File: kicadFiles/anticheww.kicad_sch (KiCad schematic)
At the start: 436 parts, among them J1 ARM JTAG, J2 TYPE-C-31-M-12, J3 Conn_02x05_Odd_Even, Q1 AO3401A, Q2 DTC123JKAT146, Q3 DTC123JKAT146, SW1 ESC, SW10 9, SW11 0, SW12 MINUS, SW13 PLUS, SW14 LBKSP, SW15 RBKSP, SW16 2U_BKSP, SW17 TAB, SW18 Q, SW19 W, SW2 1, SW20 E, SW21 R, SW22 T, SW23 Y, SW24 U, SW25 I, SW26 O, SW27 P, SW28 LBRKT, SW29 RBRKT, SW3 2, SW30 BKSLSH, SW31 PGUP, SW32 ISO_ENTER, SW33 CAPS, SW34 A, SW35 S, SW36 D, SW37 F, SW38 G, SW39 H, SW4 3, SW40 J, SW41 K, SW42 L, SW43 COLON, SW44 QUOTE, SW45 ENTER, SW46 HOME, SW47 PGDN, SW48 STEPPED_CAPS, SW49 ISO_TILDE, SW5 4, SW50 LSHFT, SW51 ISO_BKLSH, SW52 Z, SW53 X, SW54 C, SW55 V, SW56 B, SW57 N, SW58 M, SW59 COMMA, SW6 5, SW60 DOT, SW61 SLSH, SW62 175_RSHFT, SW63 UP, SW64 END, SW65 ISO_LSHFT, SW66 275_RSHFT, SW67 LCTRL_125, SW68 LGUI_125, SW69 LALT_125, SW7 6, SW70 SPC_625, SW71 RALT_100, SW72 RGUI_100, SW73 RCTRL_100, SW74 LEFT, SW75 DOWN, SW76 RIGHT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

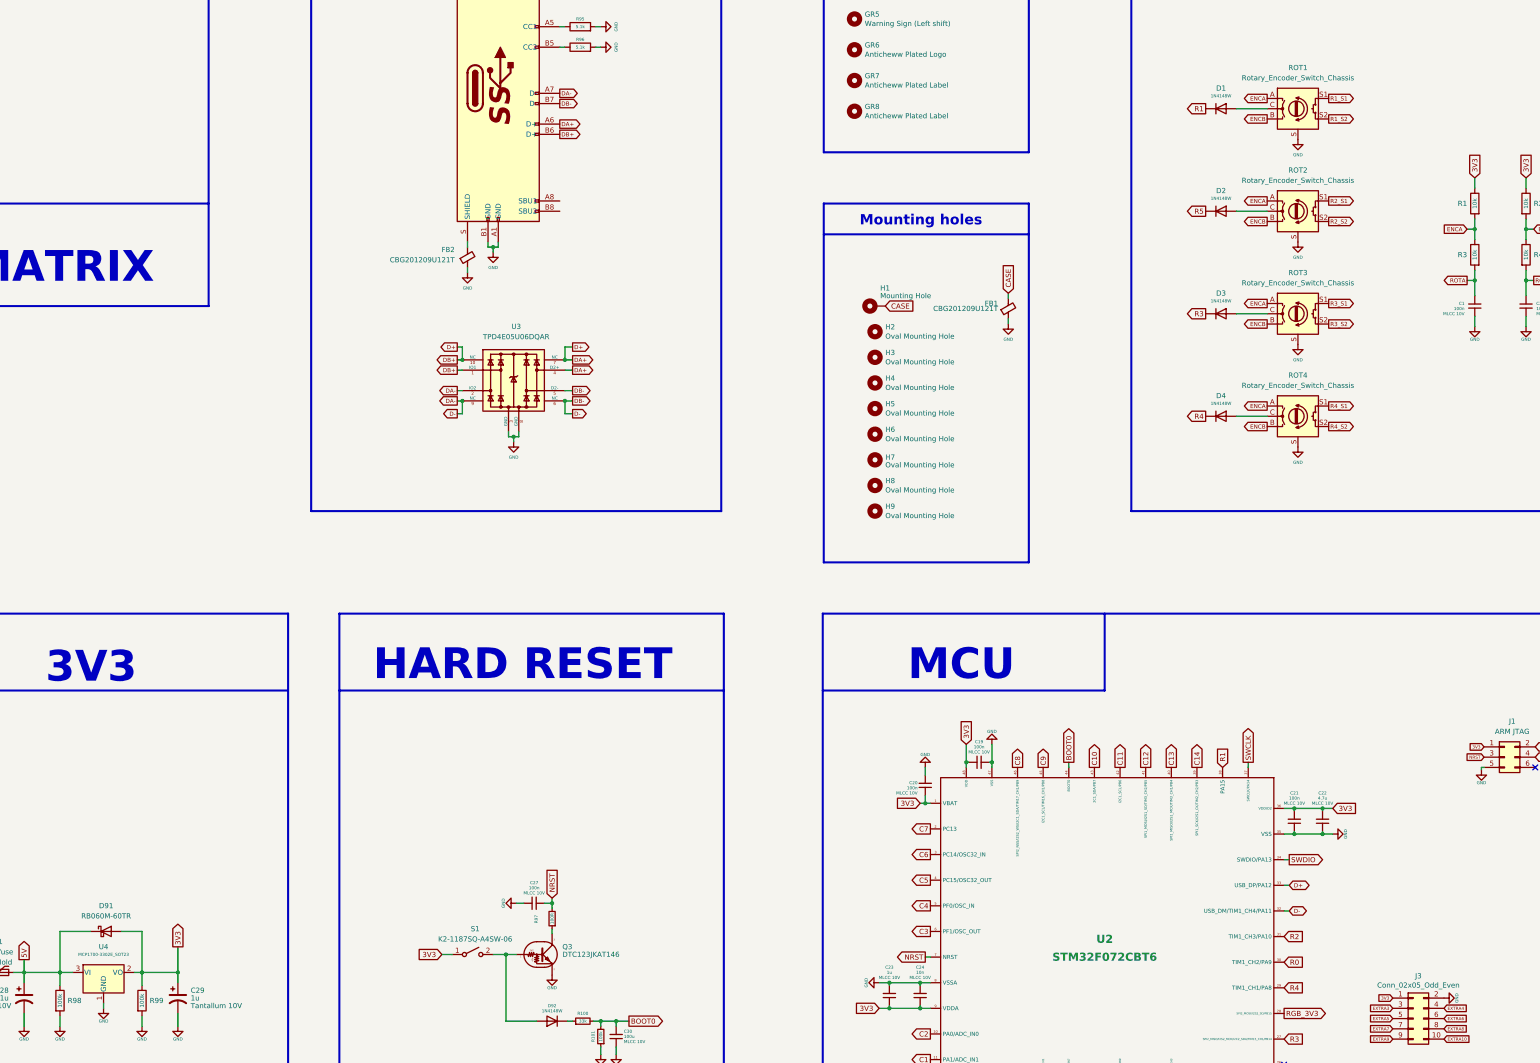
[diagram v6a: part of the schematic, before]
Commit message: Add missing maufacturer and part number to components
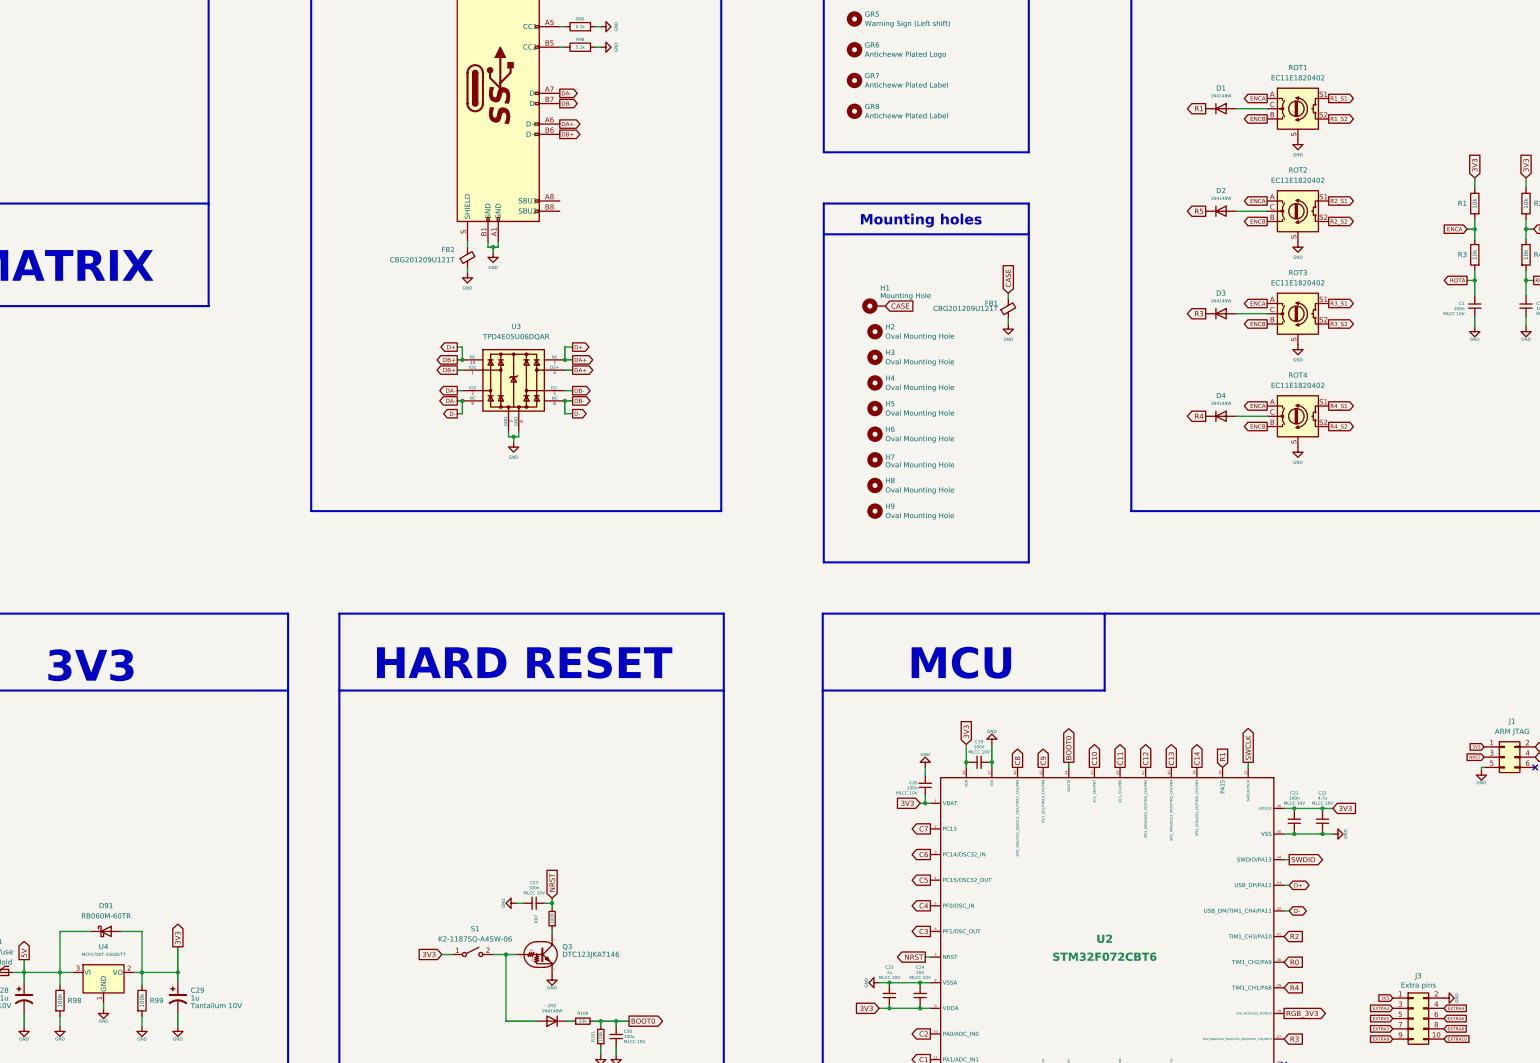
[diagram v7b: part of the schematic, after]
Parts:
- J1: Specification (none) -> 2.54mm pitch 2x3 through hole pin header
- J3: value Conn_02x05_Odd_Even -> Extra pins; Specification (none) -> 1mm pitch 2x5 through hole pin header
- ROT1: value Rotary_Encoder_Switch_Chassis -> EC11E1820402; LCSC Part Number (none) -> C361167; Manufacturer (none) -> ALPS Electric; Manufacturer Part Number (none) -> EC11E1820402; Specification (none) -> Vertical shaft rotary encoder with click switch
- ROT2, ROT3, ROT4: value Rotary_Encoder_Switch_Chassis -> EC11E1820402; LCSC Part Number (none) -> C361167; Manufacturer (none) -> ALPS Electric; Manufacturer Part Number (none) -> EC11E1820402
- U2: LCSC Part Number (none) -> C81720; Manufacturer (none) -> STMicroelectronics; Manufacturer Part Number (none) -> STM32F072CBT6; Package (none) -> LQFP-48
- U3: Manufacturer (none) -> Texas Instruments; Package (none) -> uSON-10
- U4: value MCP1700-3302E_SOT23 -> MCP1700T-3302E/TT; LCSC Part Number (none) -> C39051; Manufacturer (none) -> Microchip; Manufacturer Part Number (none) -> MCP1700T-3302E/TT; Package (none) -> SOT-23
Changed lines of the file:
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@@
-(kicad_sch (version 20200714) (host eeschema "(5.99.0-2501-gba537209a)")
-  (page 1 1)
+(kicad_sch (version 20200714) (host eeschema "(5.99.0-2523-g07085345e)")
+  (page 0 1)
   (paper "A1")
   (title_block
@@
   (junction (at 783.59 285.75) (diameter 1.016) (color 0 0 0 0))
   (junction (at 783.59 298.45) (diameter 1.016) (color 0 0 0 0))
-  (no_connect (at 785.876 419.1))
   (no_connect (at 723.646 492.76))
+  (no_connect (at 785.876 419.1))
   (wire (pts (xy 57.15 50.8) (xy 76.2 50.8))
     (stroke (width 0) (type solid) (color 0 0 0 0))
@@
   )
   (polyline (pts (xy 55.88 185.42) (xy 55.88 208.28))
-    (stroke (width 0.762) (type dot) (color 0 0 0 0))
+    (stroke (width 0.762) (type dash) (color 4 255 67 1))
   )
   (polyline (pts (xy 55.88 185.42) (xy 142.24 185.42))
-    (stroke (width 0.762) (type dot) (color 0 0 0 0))
+    (stroke (width 0.762) (type dash) (color 4 255 67 1))
   )
   (polyline (pts (xy 55.88 210.82) (xy 55.88 231.14))
-    (stroke (width 0.762) (type dot) (color 0 0 0 0))
+    (stroke (width 0.762) (type dash) (color 4 255 67 1))
   )
   (polyline (pts (xy 55.88 210.82) (xy 142.24 210.82))
-    (stroke (width 0.762) (type dot) (color 0 0 0 0))
+    (stroke (width 0.762) (type dash) (color 4 255 67 1))
   )
   (polyline (pts (xy 142.24 185.42) (xy 142.24 208.28))
-    (stroke (width 0.762) (type dot) (color 0 0 0 0))
+    (stroke (width 0.762) (type dash) (color 4 255 67 1))
   )
   (polyline (pts (xy 142.24 208.28) (xy 55.88 208.28))
-    (stroke (width 0.762) (type dot) (color 0 0 0 0))
+    (stroke (width 0.762) (type dash) (color 4 255 67 1))
   )
   (polyline (pts (xy 142.24 210.82) (xy 142.24 231.14))
-    (stroke (width 0.762) (type dot) (color 0 0 0 0))
+    (stroke (width 0.762) (type dash) (color 4 255 67 1))
   )
   (polyline (pts (xy 142.24 231.14) (xy 55.88 231.14))
-    (stroke (width 0.762) (type dot) (color 0 0 0 0))
+    (stroke (width 0.762) (type dash) (color 4 255 67 1))
   )
   (polyline (pts (xy 157.48 236.22) (xy 157.48 256.54))
@@
       (effects (font (size 1.27 1.27)) hide)
     )
+    (property "Specification" "2.54mm pitch 2x3 through hole pin header" (id 4) (at 778.256 416.56 0)
+      (effects (font (size 1.27 1.27)) hide)
+    )
   )
   (symbol (lib_id "Transistor_FET:AO3401A") (at 73.025 393.065 0) (mirror x) (unit 1)
@@
     (in_bom yes) (on_board yes)
     (property "Reference" "U4" (id 0) (at 431.165 463.55 0))
-    (property "Value" "MCP1700-3302E_SOT23" (id 1) (at 431.165 465.455 0)
+    (property "Value" "MCP1700T-3302E/TT" (id 1) (at 431.165 465.455 0)
       (effects (font (size 0.762 0.762)))
     )
@@
       (effects (font (size 1.27 1.27)) hide)
     )
+    (property "Manufacturer Part Number" "MCP1700T-3302E/TT" (id 4) (at 431.165 469.9 0)
+      (effects (font (size 1.27 1.27)) hide)
+    )
+    (property "Manufacturer" "Microchip" (id 5) (at 431.165 469.9 0)
+      (effects (font (size 1.27 1.27)) hide)
+    )
+    (property "Package" "SOT-23" (id 6) (at 431.165 469.9 0)
+      (effects (font (size 1.27 1.27)) hide)
+    )
+    (property "LCSC Part Number" "C39051" (id 7) (at 431.165 469.9 0)
+      (effects (font (size 1.27 1.27)) hide)
+    )
   )
   (symbol (lib_id "Connector_Generic:Conn_02x05_Odd_Even") (at 755.65 481.33 0) (unit 1)
     (in_bom yes) (on_board yes)
     (property "Reference" "J3" (id 0) (at 756.92 470.7698 0))
-    (property "Value" "Conn_02x05_Odd_Even" (id 1) (at 756.92 473.0685 0))
+    (property "Value" "Extra pins" (id 1) (at 756.92 473.0685 0))
     (property "Footprint" "Connector_PinHeader_1.00mm:PinHeader_2x05_P1.00mm_Vertical" (id 2) (at 755.65 481.33 0)
       (effects (font (size 1.27 1.27)) hide)
@@
       (effects (font (size 1.27 1.27)) hide)
     )
+    (property "Specification" "1mm pitch 2x5 through hole pin header" (id 4) (at 755.65 481.33 0)
+      (effects (font (size 1.27 1.27)) hide)
+    )
   )
   (symbol (lib_id "acheronSymbols:Rotary_Encoder_Switch_Chassis") (at 727.075 255.905 0) (unit 1)
     (in_bom yes) (on_board yes)
     (property "Reference" "ROT1" (id 0) (at 727.075 245.745 0))
-    (property "Value" "Rotary_Encoder_Switch_Chassis" (id 1) (at 727.075 248.285 0))
+    (property "Value" "EC11E1820402" (id 1) (at 727.075 248.285 0))
     (property "Footprint" "acheron_Hardware:ALPS_EC11E" (id 2) (at 723.265 251.841 0)
       (effects (font (size 1.27 1.27)) hide)
@@
       (effects (font (size 1.27 1.27)) hide)
     )
+    (property "Manufacturer" "ALPS Electric" (id 4) (at 727.075 255.905 0)
+      (effects (font (size 1.27 1.27)) hide)
+    )
+    (property "Manufacturer Part Number" "EC11E1820402" (id 5) (at 727.075 255.905 0)
+      (effects (font (size 1.27 1.27)) hide)
+    )
+    (property "LCSC Part Number" "C361167" (id 6) (at 727.075 255.905 0)
+      (effects (font (size 1.27 1.27)) hide)
+    )
+    (property "Specification" "Vertical shaft rotary encoder with click switch" (id 7) (at 727.075 255.905 0)
+      (effects (font (size 1.27 1.27)) hide)
+    )
   )
   (symbol (lib_id "acheronSymbols:Rotary_Encoder_Switch_Chassis") (at 727.075 281.305 0) (unit 1)
     (in_bom yes) (on_board yes)
     (property "Reference" "ROT2" (id 0) (at 727.075 271.145 0))
-    (property "Value" "Rotary_Encoder_Switch_Chassis" (id 1) (at 727.075 273.685 0))
+    (property "Value" "EC11E1820402" (id 1) (at 727.075 273.685 0))
     (property "Footprint" "acheron_Hardware:ALPS_EC11E" (id 2) (at 723.265 277.241 0)
       (effects (font (size 1.27 1.27)) hide)
@@
       (effects (font (size 1.27 1.27)) hide)
     )
+    (property "Manufacturer" "ALPS Electric" (id 4) (at 727.075 281.305 0)
+      (effects (font (size 1.27 1.27)) hide)
+    )
+    (property "Manufacturer Part Number" "EC11E1820402" (id 5) (at 727.075 281.305 0)
+      (effects (font (size 1.27 1.27)) hide)
+    )
+    (property "LCSC Part Number" "C361167" (id 6) (at 727.075 281.305 0)
+      (effects (font (size 1.27 1.27)) hide)
+    )
+    (property "Value" "EC11E1820402" (id 7) (at 727.075 281.305 0)
+      (effects (font (size 1.27 1.27)) hide)
+    )
   )
   (symbol (lib_id "acheronSymbols:Rotary_Encoder_Switch_Chassis") (at 727.075 306.705 0) (unit 1)
     (in_bom yes) (on_board yes)
     (property "Reference" "ROT3" (id 0) (at 727.075 296.545 0))
-    (property "Value" "Rotary_Encoder_Switch_Chassis" (id 1) (at 727.075 299.085 0))
+    (property "Value" "EC11E1820402" (id 1) (at 727.075 299.085 0))
     (property "Footprint" "acheron_Hardware:ALPS_EC11E" (id 2) (at 723.265 302.641 0)
       (effects (font (size 1.27 1.27)) hide)
@@
       (effects (font (size 1.27 1.27)) hide)
     )
+    (property "Manufacturer" "ALPS Electric" (id 4) (at 727.075 306.705 0)
+      (effects (font (size 1.27 1.27)) hide)
+    )
+    (property "Manufacturer Part Number" "EC11E1820402" (id 5) (at 727.075 306.705 0)
+      (effects (font (size 1.27 1.27)) hide)
+    )
+    (property "LCSC Part Number" "C361167" (id 6) (at 727.075 306.705 0)
+      (effects (font (size 1.27 1.27)) hide)
+    )
+    (property "Value" "EC11E1820402" (id 7) (at 727.075 306.705 0)
+      (effects (font (size 1.27 1.27)) hide)
+    )
   )
   (symbol (lib_id "acheronSymbols:Rotary_Encoder_Switch_Chassis") (at 727.075 332.105 0) (unit 1)
     (in_bom yes) (on_board yes)
     (property "Reference" "ROT4" (id 0) (at 727.075 321.945 0))
-    (property "Value" "Rotary_Encoder_Switch_Chassis" (id 1) (at 727.075 324.485 0))
+    (property "Value" "EC11E1820402" (id 1) (at 727.075 324.485 0))
     (property "Footprint" "acheron_Hardware:ALPS_EC11E" (id 2) (at 723.265 328.041 0)
       (effects (font (size 1.27 1.27)) hide)
@@
       (effects (font (size 1.27 1.27)) hide)
     )
+    (property "Manufacturer" "ALPS Electric" (id 4) (at 727.075 332.105 0)
+      (effects (font (size 1.27 1.27)) hide)
+    )
+    (property "Manufacturer Part Number" "EC11E1820402" (id 5) (at 727.075 332.105 0)
+      (effects (font (size 1.27 1.27)) hide)
+    )
+    (property "LCSC Part Number" "C361167" (id 6) (at 727.075 332.105 0)
+      (effects (font (size 1.27 1.27)) hide)
+    )
+    (property "Value" "EC11E1820402" (id 7) (at 727.075 332.105 0)
+      (effects (font (size 1.27 1.27)) hide)
+    )
   )
   (symbol (lib_id "acheronSymbols:MXSwitch") (at 76.2 69.85 0) (unit 1)
@@
       (effects (font (size 1.27 1.27)) hide)
     )
+    (property "Manufacturer" "Texas Instruments" (id 6) (at 532.765 323.215 0)
+      (effects (font (size 1.27 1.27)) hide)
+    )
+    (property "Package" "uSON-10" (id 7) (at 532.765 323.215 0)
+      (effects (font (size 1.27 1.27)) hide)
+    )
   )
   (symbol (lib_id "acheronSymbols:TYPE-C-31-M12_13") (at 528.955 252.095 0) (unit 1)
@@
       (effects (font (size 1.27 1.27)) hide)
     )
+    (property "Manufacturer" "STMicroelectronics" (id 4) (at 679.196 463.55 0)
+      (effects (font (size 1.27 1.27)) hide)
+    )
+    (property "Manufacturer Part Number" "STM32F072CBT6" (id 5) (at 679.196 463.55 0)
+      (effects (font (size 1.27 1.27)) hide)
+    )
+    (property "Package" "LQFP-48" (id 6) (at 679.196 463.55 0)
+      (effects (font (size 1.27 1.27)) hide)
+    )
+    (property "LCSC Part Number" "C81720" (id 7) (at 679.196 463.55 0)
+      (effects (font (size 1.27 1.27)) hide)
+    )
